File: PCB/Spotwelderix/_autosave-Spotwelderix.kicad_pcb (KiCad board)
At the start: 2 copper layers, 100 x 70 mm, 65 parts, among them IC1 INA213AIDCKR, IC2 IXDD604SIA, IC3 IXDD604SIA, J1 OnOffTast, J2 probe+, J3 Conn_01x02_Male, J4 probe-, J6 Conn_01x02_Male, P1 CONN_01X09, Q1 IRFB7430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

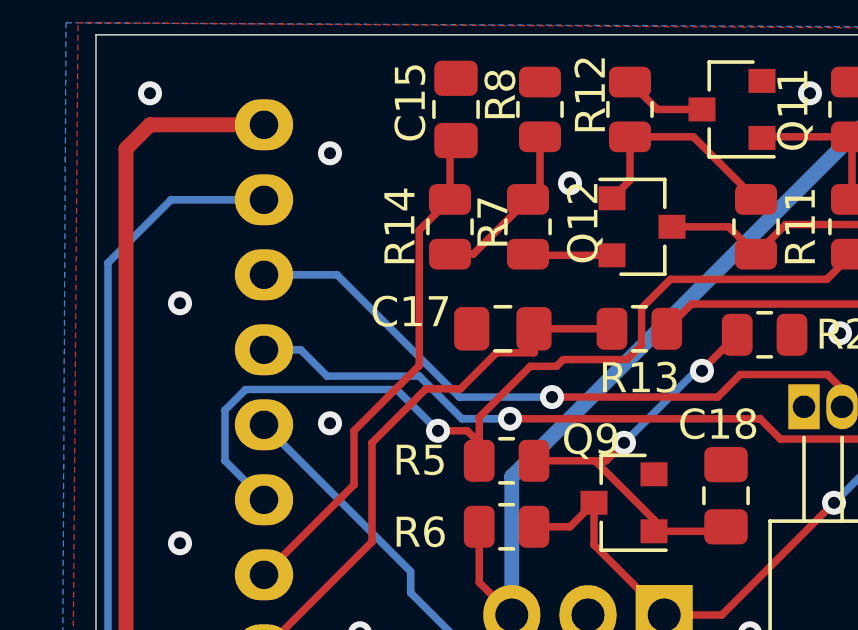
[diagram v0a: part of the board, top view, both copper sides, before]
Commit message: SW auto calibrate batt volt
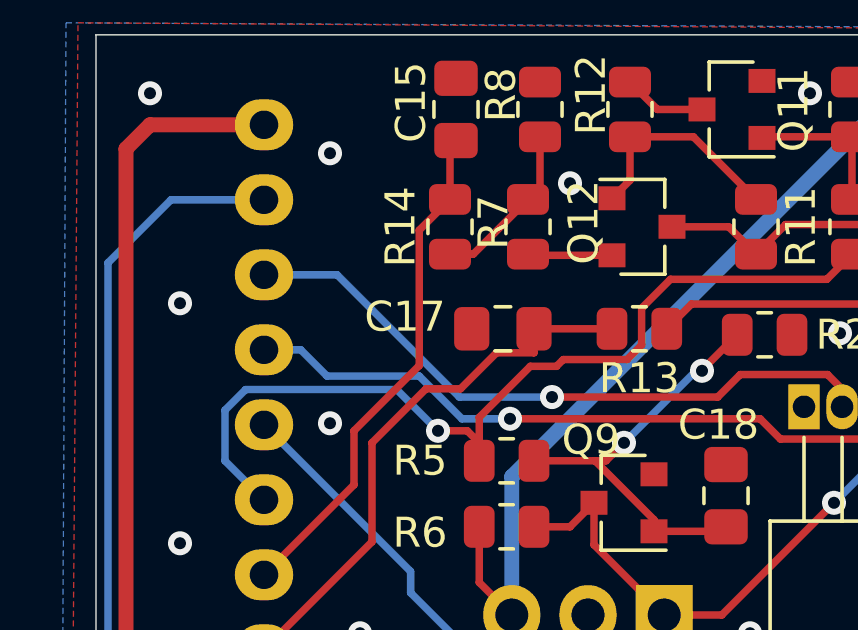
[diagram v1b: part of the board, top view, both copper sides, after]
